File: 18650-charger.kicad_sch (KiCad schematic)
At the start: 8 parts, among them J1 USB4505-03-0-A_REVA

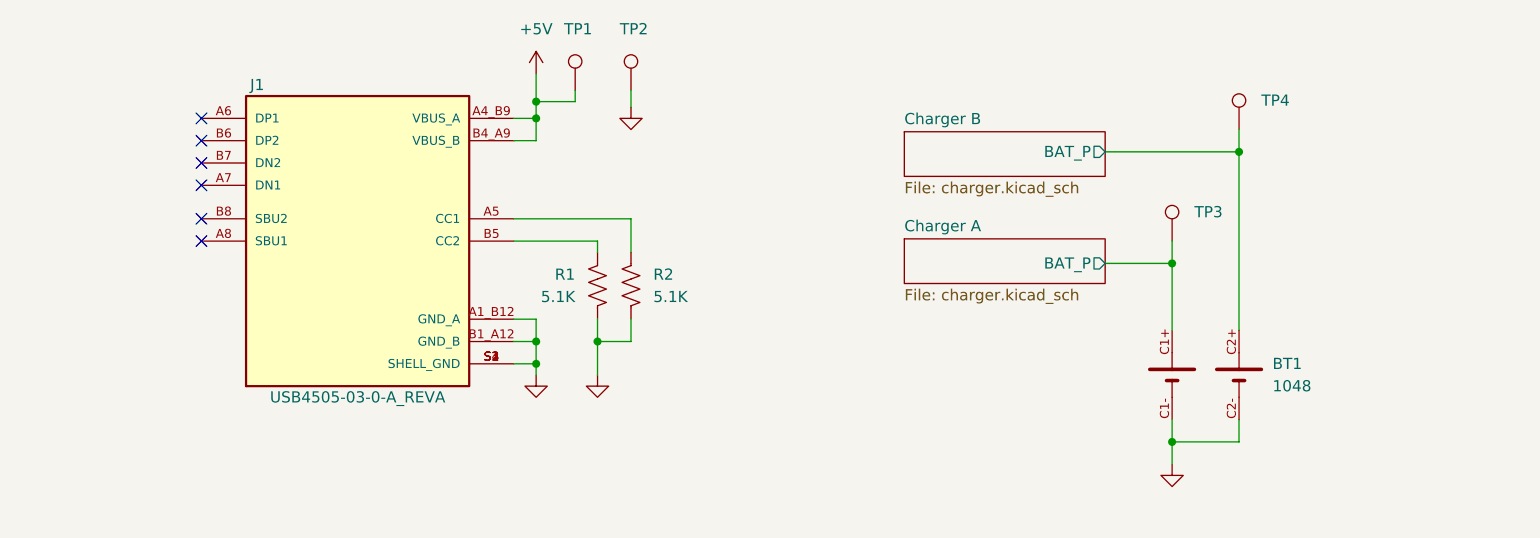
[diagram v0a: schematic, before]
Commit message: Rev 2, add ideal diode
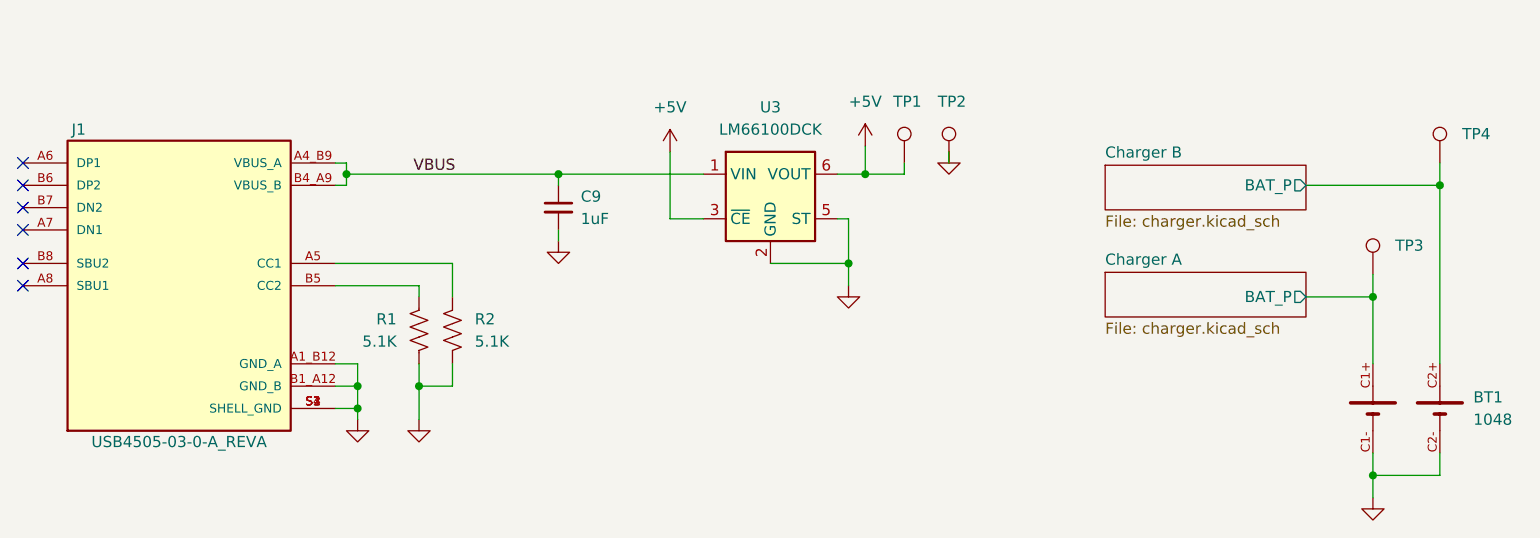
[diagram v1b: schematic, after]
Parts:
- added C9: 1uF, Capacitor_SMD:C_0402_1005Metric, symbol Device:C_Small
- added U3: LM66100DCK, Package_TO_SOT_SMD:SOT-363_SC-70-6, symbol Power_Management:LM66100DCK
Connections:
- net +5V: now also U3.3 (~{CE}), U3.6 (VOUT); no longer J1.A4_B9 (VBUS_A), J1.B4_A9 (VBUS_B)
- net GND: now also C9.2, U3.2 (GND), U3.5 (ST)
- new net VBUS: C9.1, J1.A4_B9 (VBUS_A), J1.B4_A9 (VBUS_B), U3.1 (VIN)
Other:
- moved on the sheet: BT1, J1, R1, R2, TP1, TP2, TP3, TP4
